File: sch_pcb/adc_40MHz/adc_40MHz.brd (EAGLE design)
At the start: 160 x 100 mm, 62 parts, among them IC1 LTC2227, IC2 LT6600-15, IC3 LTC6254XMS, IC5 LT1521XST, X1 SIGNAL, X2 CLK

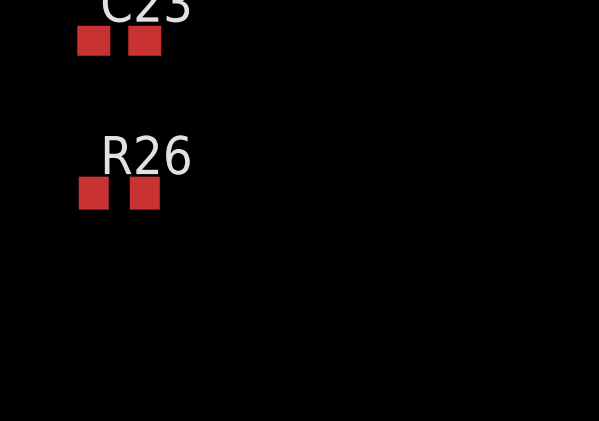
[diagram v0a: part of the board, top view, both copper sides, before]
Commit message: Drobna zmiana - dodano kondensator Vmid
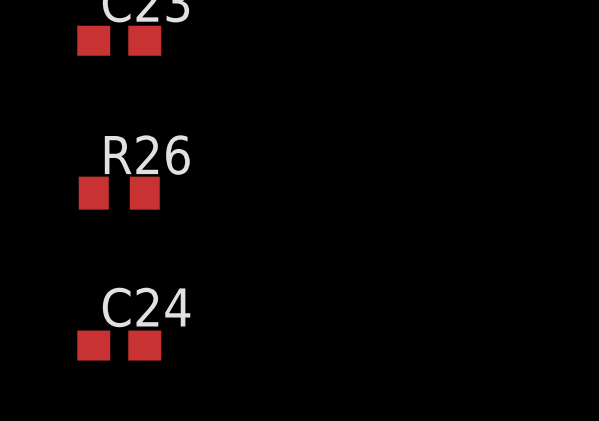
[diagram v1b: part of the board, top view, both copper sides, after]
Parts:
- added C24: 51pF, rcl:C0603
- RN4: value LT5400-1 -> LT5400-4
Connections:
- net GND: now also C24.2
- net N$18: now also C24.1
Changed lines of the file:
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@@
 <element name="R14" library="rcl" package="R0603" value="100k" x="-92.71" y="-147.32"/>
 <element name="R15" library="rcl" package="R0603" value="DNP" x="-92.71" y="-152.4"/>
-<element name="RN4" library="lt5400" package="MS8E" value="LT5400-1" x="-99.06" y="-151.13"/>
+<element name="RN4" library="lt5400" package="MS8E" value="LT5400-4" x="-99.06" y="-151.13"/>
 <element name="R16" library="rcl" package="R0603" value="270R 0.1%" x="-100.33" y="-157.48"/>
 <element name="R17" library="rcl" package="R0603" value="300R 0.1%" x="-100.33" y="-162.56"/>
@@
 <element name="C23" library="rcl" package="C0603" value="100n" x="-100.33" y="-320.04"/>
 <element name="R26" library="rcl" package="R0603" value="DNP" x="-100.33" y="-325.12"/>
+<element name="C24" library="rcl" package="C0603" value="51pF" x="-100.33" y="-330.2"/>
 </elements>
 <signals>
@@
 <contactref element="R26" pad="1"/>
 <contactref element="C23" pad="2"/>
+<contactref element="C24" pad="2"/>
 <wire x1="-98.085" y1="-153.18" x2="-99.06" y2="-151.13" width="0" layer="19" extent="1-1"/>
 <wire x1="-93.56" y1="-152.4" x2="-98.085" y2="-153.18" width="0" layer="19" extent="1-1"/>
@@
 <wire x1="-99.48" y1="-320.04" x2="-98.11" y2="-303.53" width="0" layer="19" extent="1-1"/>
 <wire x1="-101.18" y1="-325.12" x2="-99.48" y2="-320.04" width="0" layer="19" extent="1-1"/>
+<wire x1="-99.48" y1="-330.2" x2="-101.18" y2="-325.12" width="0" layer="19" extent="1-1"/>
 </signal>
 <signal name="N$1">
@@
 <contactref element="IC2" pad="7"/>
 <contactref element="IC3" pad="12"/>
+<contactref element="C24" pad="1"/>
 <wire x1="-90.805" y1="-96.46" x2="-89.92" y2="-104.53" width="0" layer="19" extent="1-1"/>
+<wire x1="-101.18" y1="-330.2" x2="-89.92" y2="-104.53" width="0" layer="19" extent="1-1"/>
 </signal>
 <signal name="N$26">
